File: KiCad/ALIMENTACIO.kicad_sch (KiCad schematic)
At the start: 17 parts, among them J1 Conn_01x02_Pin, U1 LM2596S-5, U2 LM1117DT-3.3

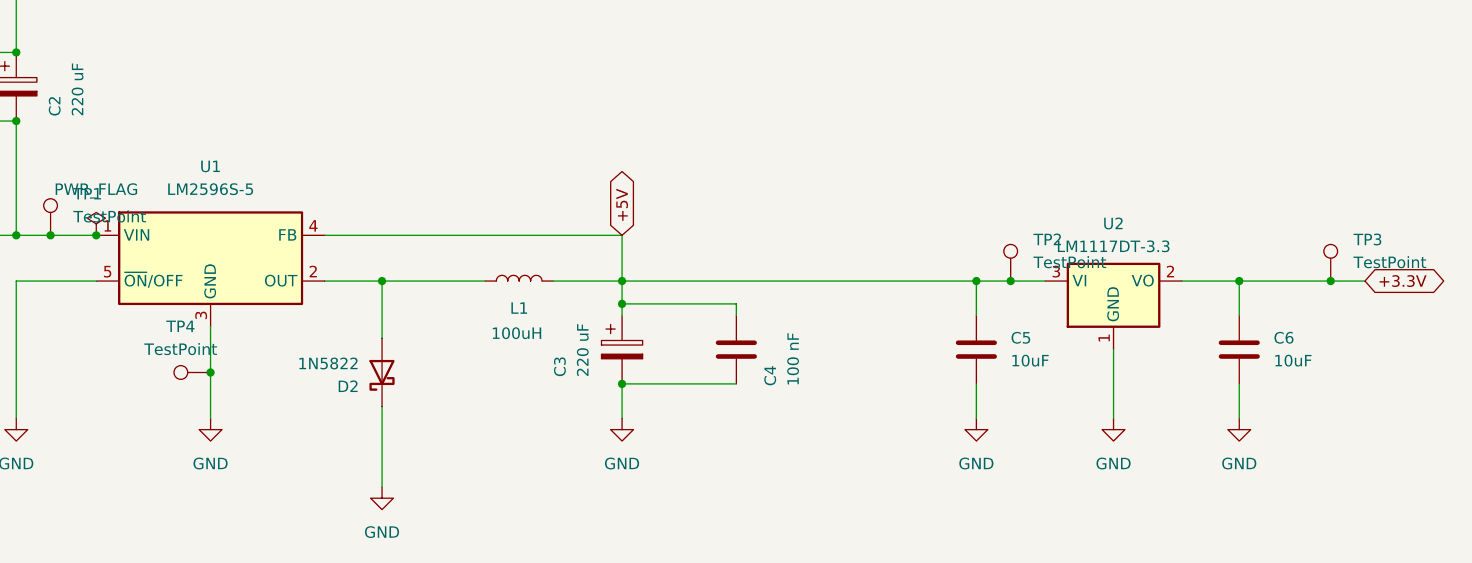
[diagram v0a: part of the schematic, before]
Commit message: Modificat ETIQUETES MICROCONTROLADOR i errors varis
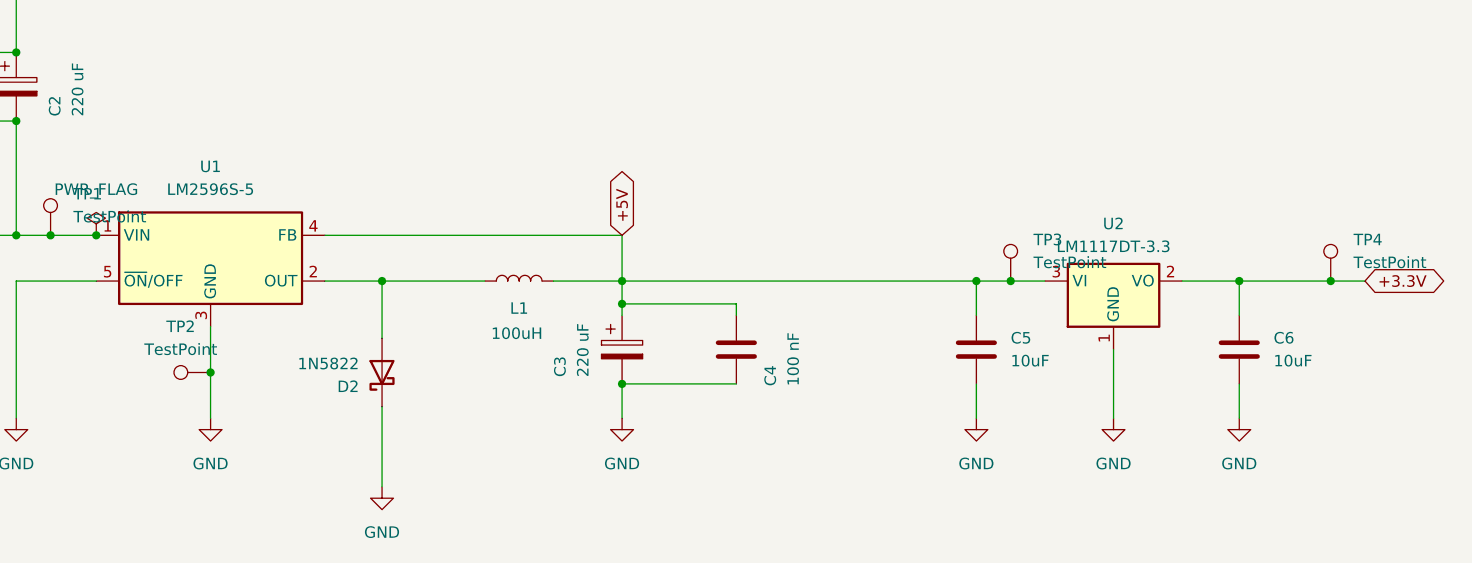
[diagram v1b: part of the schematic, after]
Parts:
- renumbered TP4 to TP2, TP2 to TP3, TP3 to TP4
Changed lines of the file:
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@@
 		(dnp no)
 		(fields_autoplaced yes)
-		(property "Reference" "TP?"
+		(property "Reference" "TP2"
 			(at 127.508 109.22 90)
 			(effects
@@
 			(project "SEIENTS_EDD"
 				(path "/b6401b4f-5426-49b8-bb2e-8ecdb19989ef/67d546eb-b5d9-4a2c-a3ee-41df96785a31"
-					(reference "TP?")
+					(reference "TP2")
 					(unit 1)
 				)
@@
 		(dnp no)
 		(fields_autoplaced yes)
-		(property "Reference" "TP?"
+		(property "Reference" "TP4"
 			(at 257.81 99.5679 0)
 			(effects
@@
 			(project "SEIENTS_EDD"
 				(path "/b6401b4f-5426-49b8-bb2e-8ecdb19989ef/67d546eb-b5d9-4a2c-a3ee-41df96785a31"
-					(reference "TP?")
+					(reference "TP4")
 					(unit 1)
 				)
@@
 		(dnp no)
 		(fields_autoplaced yes)
-		(property "Reference" "TP?"
+		(property "Reference" "TP1"
 			(at 115.57 94.4879 0)
 			(effects
@@
 			(project "SEIENTS_EDD"
 				(path "/b6401b4f-5426-49b8-bb2e-8ecdb19989ef/67d546eb-b5d9-4a2c-a3ee-41df96785a31"
-					(reference "TP?")
+					(reference "TP1")
 					(unit 1)
 				)
@@
 		(dnp no)
 		(fields_autoplaced yes)
-		(property "Reference" "TP?"
+		(property "Reference" "TP3"
 			(at 222.25 99.5679 0)
 			(effects
@@
 			(project "SEIENTS_EDD"
 				(path "/b6401b4f-5426-49b8-bb2e-8ecdb19989ef/67d546eb-b5d9-4a2c-a3ee-41df96785a31"
-					(reference "TP?")
-					(unit 1)
-				)
+					(reference "TP3")
+					(unit 1)
+				)

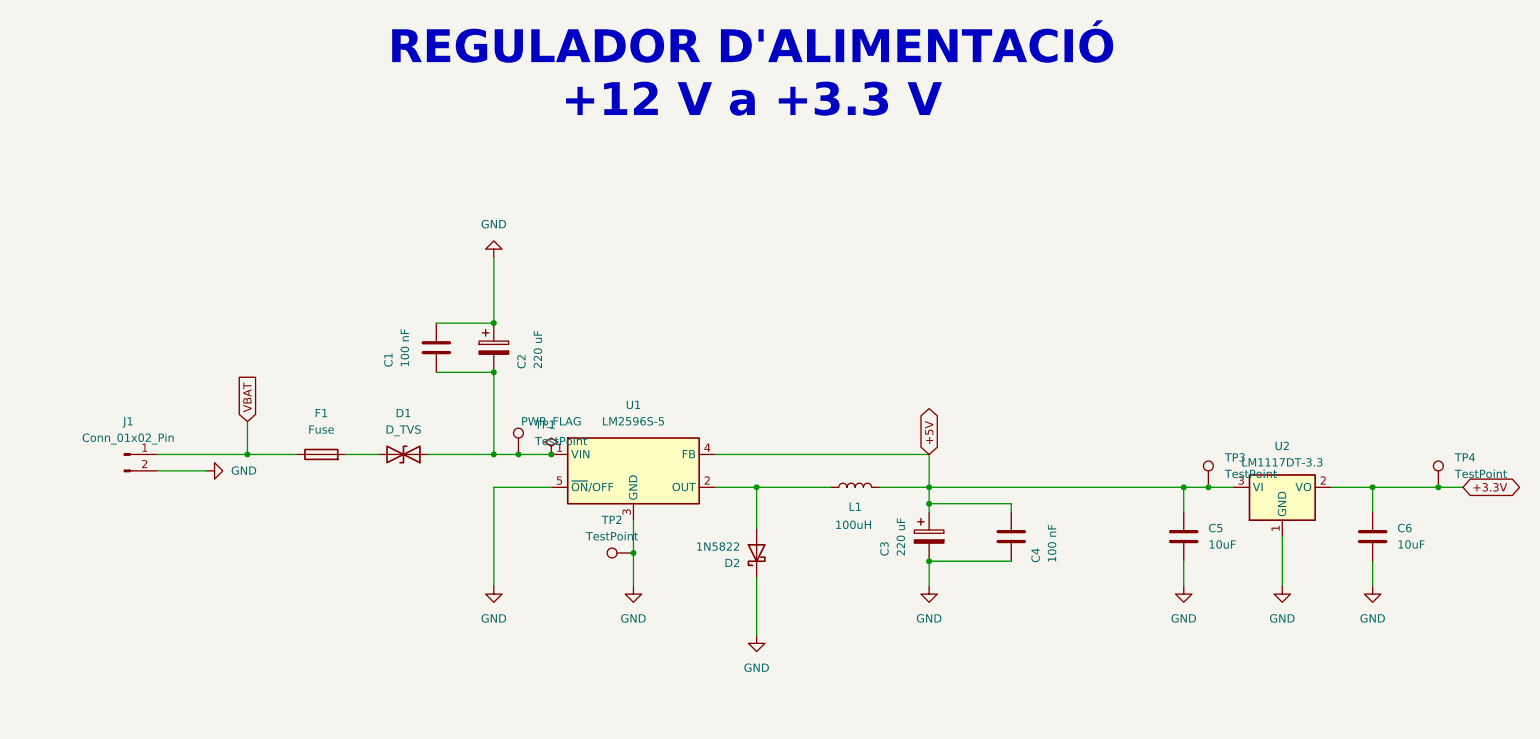
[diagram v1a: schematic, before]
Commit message: Organització Esquematic, asignacio huellas Test Points i Microcontrolador acabat
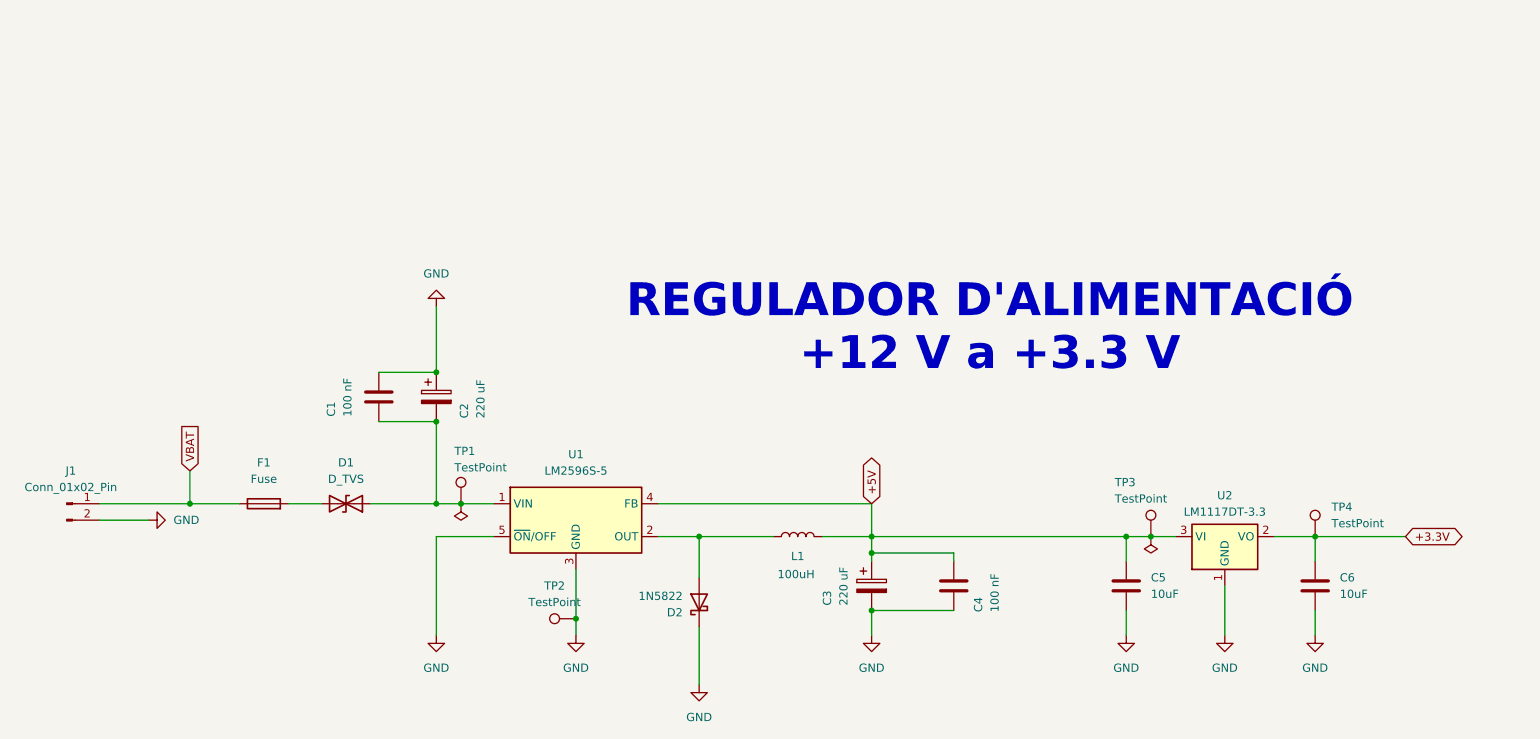
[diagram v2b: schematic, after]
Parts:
- TP1, TP2, TP3, TP4: footprint (none) -> TestPoint:TestPoint_Pad_D1.0mm
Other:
- moved on the sheet: C1, C2, C3, C4, C5, C6, D1, D2, F1, J1, L1, TP1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

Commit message: Modificació als ALIMENTACIÓ
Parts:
- renumbered D2 to D1, D1 to D2, TP3 to TP2, TP4 to TP3, TP2 to TP4
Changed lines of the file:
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@@
+	)
+	(junction
+		(at 55.88 109.22)
+		(diameter 0)
+		(color 0 0 0 0)
 	)
 	(junction
@@
 		(color 0 0 0 0)
 	)
+	(junction
+		(at 214.63 111.76)
+		(diameter 0)
+		(color 0 0 0 0)
+	)
 	(wire
 		(pts
@@
 		(dnp no)
 		(fields_autoplaced yes)
-		(property "Reference" "TP2"
+		(property "Reference" "TP4"
 			(at 118.618 119.38 90)
 			(effects
@@
 		(dnp no)
 		(fields_autoplaced yes)
-		(property "Reference" "D1"
+		(property "Reference" "D2"
 			(at 86.36 100.33 0)
 			(effects
@@
 		(dnp no)
 		(fields_autoplaced yes)
-		(property "Reference" "TP4"
+		(property "Reference" "TP3"
 			(at 238.76 107.1879 0)
 			(effects
@@
 	)
 	(symbol
-		(lib_id "power:PWR_FLAG")
-		(at 210.82 111.76 180)
-		(unit 1)
-		(exclude_from_sim no)
-		(in_bom yes)
-		(on_board yes)
-		(dnp no)
-		(property "Reference" "#FLG07"
-			(at 210.82 113.665 0)
-			(effects
-				(font
-					(size 1.27 1.27)
-				)
-				(hide yes)
-			)
-		)
-		(property "Value" "PWR_FLAG"
-			(at 210.82 115.062 0)
-			(effects
-				(font
-					(size 1.27 1.27)
-				)
-				(hide yes)
-			)
-		)
-		(property "Footprint" ""
-			(at 210.82 111.76 0)
-			(effects
-				(font
-					(size 1.27 1.27)
-				)
-				(hide yes)
-			)
-		)
-		(property "Datasheet" "~"
-			(at 210.82 111.76 0)
-			(effects
-				(font
-					(size 1.27 1.27)
-				)
-				(hide yes)
-			)
-		)
-		(property "Description" "Special symbol for telling ERC where power comes from"
-			(at 210.82 111.76 0)
-			(effects
-				(font
-					(size 1.27 1.27)
-				)
-				(hide yes)
-			)
-		)
-		(pin "1"
-		)
-		(instances
-			(project ""
-				(path "/b6401b4f-5426-49b8-bb2e-8ecdb19989ef/67d546eb-b5d9-4a2c-a3ee-41df96785a31"
-					(reference "#FLG07")
-					(unit 1)
-				)
-			)
-		)
-	)
-	(symbol
 		(lib_id "power:GND")
 		(at 167.64 127 0)
@@
 		(dnp no)
 		(fields_autoplaced yes)
-		(property "Reference" "#PWR06"
+		(property "Reference" "#PWR05"
 			(at 167.64 133.35 0)
 			(effects
@@
 		(dnp no)
 		(fields_autoplaced yes)
-		(property "Reference" "D2"
+		(property "Reference" "D1"
 			(at 138.43 123.5076 90)
 			(effects
@@
 		(dnp no)
 		(fields_autoplaced yes)
-		(property "Reference" "#PWR03"
+		(property "Reference" "#PWR02"
 			(at 100.33 133.35 0)
 			(effects
@@
 		(dnp no)
 		(fields_autoplaced yes)
-		(property "Reference" "#PWR09"
+		(property "Reference" "#PWR08"
 			(at 236.22 133.35 0)
 			(effects
@@
 		(dnp no)
 		(fields_autoplaced yes)
-		(property "Reference" "#PWR08"
+		(property "Reference" "#PWR07"
 			(at 222.25 133.35 0)
 			(effects
@@
 		(dnp no)
 		(fields_autoplaced yes)
-		(property "Reference" "#PWR04"
+		(property "Reference" "#PWR03"
 			(at 121.92 133.35 0)
 			(effects
@@
 		(on_board yes)
 		(dnp no)
-		(property "Reference" "TP3"
+		(property "Reference" "TP2"
 			(at 205.232 103.378 0)
 			(effects
@@
 		(dnp no)
 		(fields_autoplaced yes)
-		(property "Reference" "#PWR07"
+		(property "Reference" "#PWR06"
 			(at 207.01 133.35 0)
 			(effects
@@
 	)
 	(symbol
+		(lib_id "power:PWR_FLAG")
+		(at 214.63 111.76 180)
+		(unit 1)
+		(exclude_from_sim no)
+		(in_bom yes)
+		(on_board yes)
+		(dnp no)
+		(fields_autoplaced yes)
+		(property "Reference" "#FLG03"
+			(at 214.63 113.665 0)
+			(effects
+				(font
+					(size 1.27 1.27)
+				)
+				(hide yes)
+			)
+		)
+		(property "Value" "PWR_FLAG"
+			(at 214.63 116.84 0)
+			(effects
+				(font
+					(size 1.27 1.27)
+				)
+			)
+		)
+		(property "Footprint" ""
+			(at 214.63 111.76 0)
+			(effects
+				(font
+					(size 1.27 1.27)
+				)
+				(hide yes)
+			)
+		)
+		(property "Datasheet" "~"
+			(at 214.63 111.76 0)
+			(effects
+				(font
+					(size 1.27 1.27)
+				)
+				(hide yes)
+			)
+		)
+		(property "Description" "Special symbol for telling ERC where power comes from"
+			(at 214.63 111.76 0)
+			(effects
+				(font
+					(size 1.27 1.27)
+				)
+				(hide yes)
+			)
+		)
+		(pin "1"
+		)
+		(instances
+			(project "ALIMENTACIO"
+				(path "/45cfcaa5-e694-40cb-923c-70f0cad76365"
+					(reference "#FLG03")
+					(unit 1)
+				)
+			)
+		)
+	)
+	(symbol
 		(lib_id "power:GND")
 		(at 140.97 134.62 0)
@@
 		(dnp no)
 		(fields_autoplaced yes)
-		(property "Reference" "#PWR05"
+		(property "Reference" "#PWR04"
 			(at 140.97 140.97 0)
 			(effects
@@
 	(symbol
 		(lib_id "power:PWR_FLAG")
+		(at 55.88 109.22 180)
+		(unit 1)
+		(exclude_from_sim no)
+		(in_bom yes)
+		(on_board yes)
+		(dnp no)
+		(fields_autoplaced yes)
+		(property "Reference" "#FLG02"
+			(at 55.88 111.125 0)
+			(effects
+				(font
+					(size 1.27 1.27)
+				)
+				(hide yes)
+			)
+		)
+		(property "Value" "PWR_FLAG"
+			(at 55.88 114.3 0)
+			(effects
+				(font
+					(size 1.27 1.27)
+				)
+			)
+		)
+		(property "Footprint" ""
+			(at 55.88 109.22 0)
+			(effects
+				(font
+					(size 1.27 1.27)
+				)
+				(hide yes)
+			)
+		)
+		(property "Datasheet" "~"
+			(at 55.88 109.22 0)
+			(effects
+				(font
+					(size 1.27 1.27)
+				)
+				(hide yes)
+			)
+		)
+		(property "Description" "Special symbol for telling ERC where power comes from"
+			(at 55.88 109.22 0)
+			(effects
+				(font
+					(size 1.27 1.27)
+				)
+				(hide yes)
+			)
+		)
+		(pin "1"
+		)
+		(instances
+			(project ""
+				(path "/45cfcaa5-e694-40cb-923c-70f0cad76365"
+					(reference "#FLG02")
+					(unit 1)
+				)
+			)
+		)
+	)
+	(symbol
+		(lib_id "power:PWR_FLAG")
 		(at 104.14 106.68 180)
 		(unit 1)
@@
 		(dnp no)
 		(fields_autoplaced yes)
-		(property "Reference" "#FLG03"
+		(property "Reference" "#FLG01"
 			(at 104.14 108.585 0)
 			(effects
@@
 		(dnp no)
 		(fields_autoplaced yes)
-		(property "Reference" "#PWR02"
+		(property "Reference" "#PWR09"
 			(at 100.33 69.85 0)
 			(effects
